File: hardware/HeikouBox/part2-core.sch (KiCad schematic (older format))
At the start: 20 parts, among them J201 Conn_02x05_Odd_Even, U201 HeikouBox-Core, U202 74HCU04, Y201 14.31818MHz, Y202 28.37516MHz

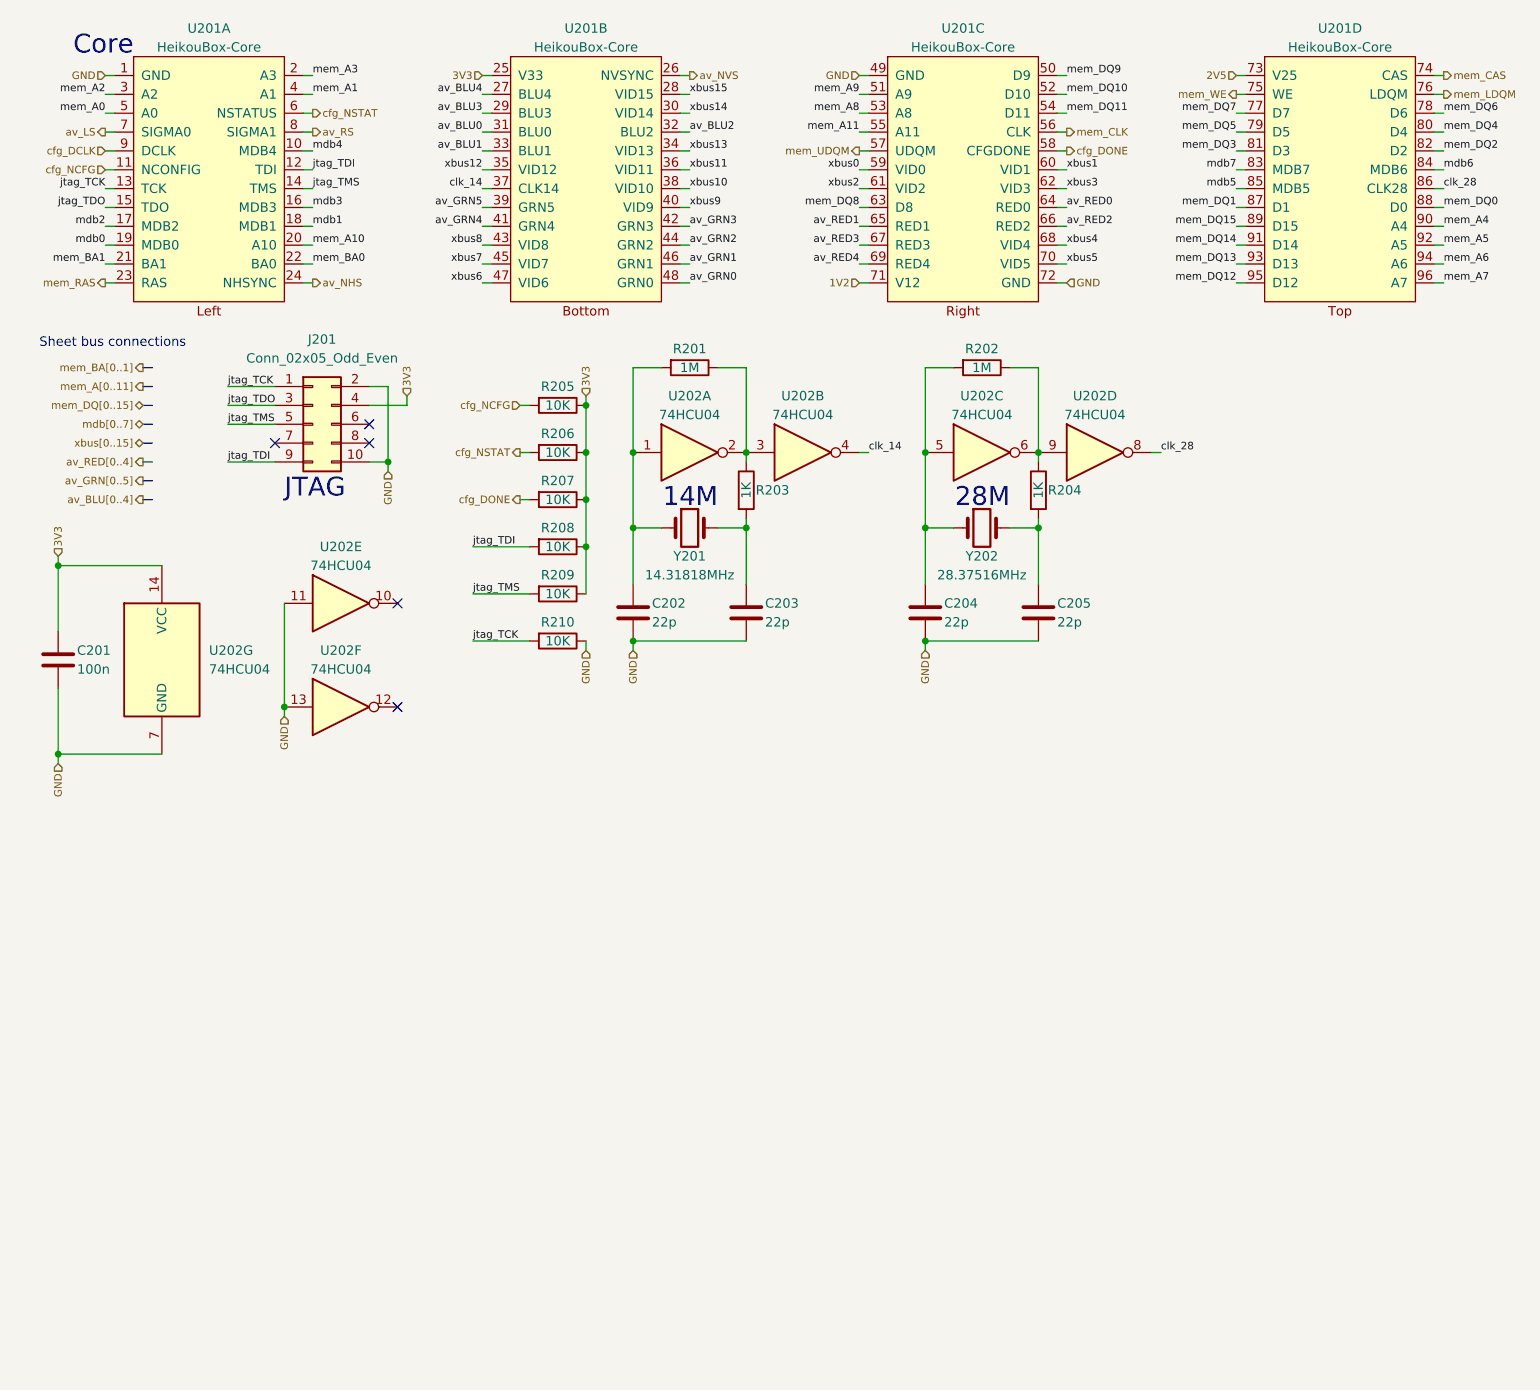
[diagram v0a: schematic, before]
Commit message: Replace MCU with blue pill, tidy up
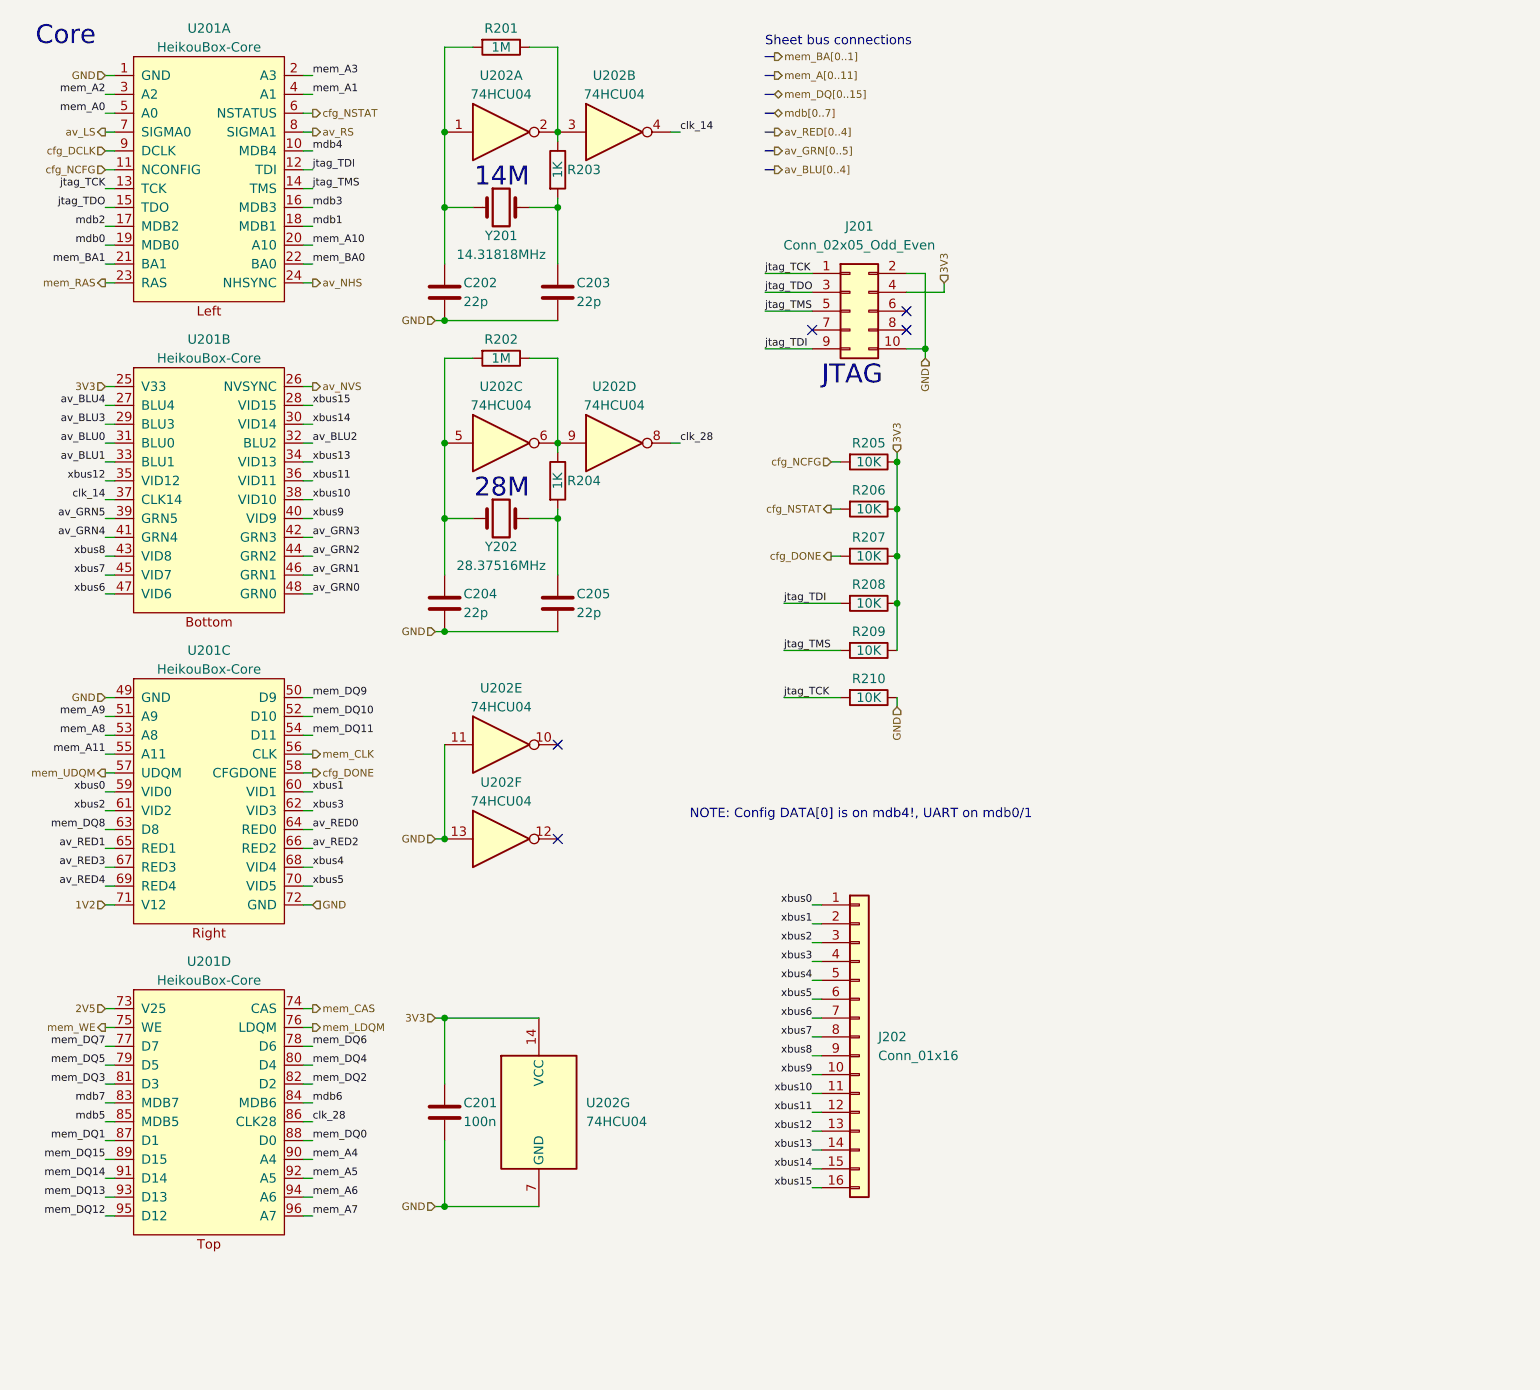
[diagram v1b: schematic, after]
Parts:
- added J202: Conn_01x16, Connector_PinSocket_2.54mm:PinSocket_1x16_P2.54mm_Vertical, symbol Connector_Generic:Conn_01x16
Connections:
- net xbus0: now also J202.1 (Pin_1)
- net xbus1: now also J202.2 (Pin_2)
- net xbus10: now also J202.11 (Pin_11)
- net xbus11: now also J202.12 (Pin_12)
- net xbus12: now also J202.13 (Pin_13)
- net xbus13: now also J202.14 (Pin_14)
- net xbus14: now also J202.15 (Pin_15)
- net xbus15: now also J202.16 (Pin_16)
- net xbus2: now also J202.3 (Pin_3)
- net xbus3: now also J202.4 (Pin_4)
- net xbus4: now also J202.5 (Pin_5)
- net xbus5: now also J202.6 (Pin_6)
- net xbus6: now also J202.7 (Pin_7)
- net xbus7: now also J202.8 (Pin_8)
- net xbus8: now also J202.9 (Pin_9)
- net xbus9: now also J202.10 (Pin_10)
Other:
- note added: "NOTE: Config DATA[0] is on mdb4!, UART on mdb0/1"
- moved on the sheet: C201, C202, C203, C204, C205, J201, R201, R202, R203, R204, R205, R206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

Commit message: Fix DRC, make netlist
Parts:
- U201: symbol KSK_HeikouBox:HeikouBox-Core -> KSK_HeikouBox:HeikouBox-Core-Socket
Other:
- moved on the sheet: C201, U202G
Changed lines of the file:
@@
 Core
 $Comp
-L KSK_HeikouBox:HeikouBox-Core U?
+L KSK_HeikouBox:HeikouBox-Core-Socket U?
 U 4 1 67C578BE
 P 1450 5650
@@
 av_BLU4
 $Comp
-L KSK_HeikouBox:HeikouBox-Core U?
+L KSK_HeikouBox:HeikouBox-Core-Socket U?
 U 2 1 67C578E9
 P 1450 2350
@@
 mdb3
 $Comp
-L KSK_HeikouBox:HeikouBox-Core U?
+L KSK_HeikouBox:HeikouBox-Core-Socket U?
 U 1 1 67C5790A
 P 1450 700
@@
 mdb6
 $Comp
-L KSK_HeikouBox:HeikouBox-Core U?
+L KSK_HeikouBox:HeikouBox-Core-Socket U?
 U 3 1 67C5791D
 P 1450 4000
@@
 $EndComp
 Wire Wire Line
-	4750 2850 4800 2850
-Wire Wire Line
-	4750 3100 4800 3100
-Wire Wire Line
-	4750 3350 4800 3350
-Wire Wire Line
-	4500 4100 4800 4100
+	4700 2850 4800 2850
+Wire Wire Line
+	4700 3100 4800 3100
+Wire Wire Line
+	4700 3350 4800 3350
+Wire Wire Line
+	4700 4100 4800 4100
 Text Notes 4700 2450 0    100  ~ 0
 JTAG
@@
 NoConn ~ 5150 2050
 NoConn ~ 5150 2150
-Wire Wire Line
-	5350 1950 5150 1950
 Wire Wire Line
 	5250 1850 5250 2250
@@
 NoConn ~ 3300 4350
 Wire Wire Line
-	2700 5800 3200 5800
+	2800 5800 3300 5800
 Wire Wire Line
 	2700 650  2700 1100
@@
 L Device:C C?
 U 1 1 67C57A73
-P 2700 6300
+P 2800 6300
 AR Path="/67C57A73" Ref="C?"  Part="1"
 AR Path="/71351D1D/67C57A73" Ref="C201"  Part="1"
 AR Path="/729F86A7/67C57A73" Ref="C?"  Part="1"
-F 0 "C201" H 2800 6350 50  0000 L CNN
-F 1 "100n" H 2800 6250 50  0000 L CNN
-F 2 "Capacitor_SMD:C_0603_1608Metric_Pad1.05x0.95mm_HandSolder" H 2738 6150 50  0001 C CNN
-F 3 "~" H 2700 6300 50  0001 C CNN
-	1    2700 6300
+F 0 "C201" H 2900 6350 50  0000 L CNN
+F 1 "100n" H 2900 6250 50  0000 L CNN
+F 2 "Capacitor_SMD:C_0603_1608Metric_Pad1.05x0.95mm_HandSolder" H 2838 6150 50  0001 C CNN
+F 3 "~" H 2800 6300 50  0001 C CNN
+	1    2800 6300
 	1    0    0    -1
 $EndComp
@@
 L 74xx:74HC04 U?
 U 7 1 67C57AA7
-P 3200 6300
+P 3300 6300
 AR Path="/67C57AA7" Ref="U?"  Part="7"
 AR Path="/71351D1D/67C57AA7" Ref="U202"  Part="7"
 AR Path="/729F86A7/67C57AA7" Ref="U?"  Part="7"
-F 0 "U202" H 3450 6350 50  0000 L CNN
-F 1 "74HCU04" H 3450 6250 50  0000 L CNN
-F 2 "Package_SO:SOIC-14_3.9x8.7mm_P1.27mm" H 3200 6300 50  0001 C CNN
-F 3 "https://assets.nexperia.com/documents/data-sheet/74HC_HCT04.pdf" H 3200 6300 50  0001 C CNN
-	7    3200 6300
+F 0 "U202" H 3550 6350 50  0000 L CNN
+F 1 "74HCU04" H 3550 6250 50  0000 L CNN
+F 2 "Package_SO:SOIC-14_3.9x8.7mm_P1.27mm" H 3300 6300 50  0001 C CNN
+F 3 "https://assets.nexperia.com/documents/data-sheet/74HC_HCT04.pdf" H 3300 6300 50  0001 C CNN
+	7    3300 6300
 	1    0    0    -1
 $EndComp
@@
 14M
 Wire Wire Line
-	5250 2300 5250 2250
-Text HLabel 5250 2300 3    40   Input ~ 0
+	5350 2250 5250 2250
+Text HLabel 5350 2250 2    40   Input ~ 0
 GND
 Connection ~ 5250 2250
-Text HLabel 4750 3350 0    40   Output ~ 0
+Text HLabel 4700 3350 0    40   Output ~ 0
 cfg_DONE
 Wire Wire Line
-	4500 3600 4800 3600
-Wire Wire Line
-	4500 3850 4800 3850
-Text HLabel 4750 3100 0    40   Output ~ 0
+	4700 3600 4800 3600
+Wire Wire Line
+	4700 3850 4800 3850
+Text HLabel 4700 3100 0    40   Output ~ 0
 cfg_NSTAT
-Text HLabel 4750 2850 0    40   Input ~ 0
+Text HLabel 4700 2850 0    40   Input ~ 0
 cfg_NCFG
 Wire Wire Line
@@
 Text HLabel 5100 2800 1    40   Input ~ 0
 3V3
-Text HLabel 5350 1900 1    40   Input ~ 0
+Text HLabel 5350 1950 2    40   Input ~ 0
 3V3
-Wire Wire Line
-	5350 1900 5350 1950
 Wire Wire Line
 	5100 4150 5100 4100
@@
 Text Label 2000 800  0    40   ~ 0
 mem_A3
-Text Label 4500 4100 0    40   ~ 0
+Text Label 4700 4100 2    40   ~ 0
 jtag_TCK
 Text Label 2000 1300 0    40   ~ 0
@@
 jtag_TDO
 Wire Wire Line
-	2700 5800 2650 5800
-Text HLabel 2650 5800 0    40   Input ~ 0
+	2800 5800 2700 5800
+Text HLabel 2700 5800 0    40   Input ~ 0
 3V3
 Wire Wire Line
 	2700 4350 2700 4850
 Wire Wire Line
-	2650 6800 2700 6800
-Text HLabel 2650 6800 0    40   Input ~ 0
+	2700 6800 2800 6800
+Text HLabel 2700 6800 0    40   Input ~ 0
 GND
 Wire Wire Line
-	3200 6800 2700 6800
-Connection ~ 2700 6800
-Wire Wire Line
-	2700 6800 2700 6450
+	3300 6800 2800 6800
+Connection ~ 2800 6800
+Wire Wire Line
+	2800 6800 2800 6450
 Wire Wire Line
 	2650 4850 2700 4850
@@
 GND
 Connection ~ 2700 4850
-Connection ~ 2700 5800
-Wire Wire Line
-	2700 6150 2700 5800
+Connection ~ 2800 5800
+Wire Wire Line
+	2800 6150 2800 5800
 Wire Wire Line
 	3150 650  3300 650
@@
 	1    0    0    -1
 $EndComp
-Text Label 4500 3850 0    40   ~ 0
+Text Label 4700 3850 2    40   ~ 0
 jtag_TMS
-Text Label 4500 3600 0    40   ~ 0
+Text Label 4700 3600 2    40   ~ 0
 jtag_TDI
 Text Notes 4000 4750 0    50   ~ 0
@@
 Text Label 4650 6700 2    40   ~ 0
 xbus15
+Wire Wire Line
+	5150 1950 5350 1950
 $EndSCHEMATC

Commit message: Mostly routed board
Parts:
- C201, C202, C203, C204, C205: footprint Capacitor_SMD:C_0603_1608Metric_Pad1.05x0.95mm_HandSolder -> Capacitor_SMD:C_0603_1608Metric_Pad1.08x0.95mm_HandSolder
- J202: value Conn_01x16 -> Conn_02x08_Odd_Even; footprint Connector_PinSocket_2.54mm:PinSocket_1x16_P2.54mm_Vertical -> Connector_PinHeader_2.54mm:PinHeader_2x08_P2.54mm_Vertical; symbol Connector_Generic:Conn_01x16 -> Connector_Generic:Conn_02x08_Odd_Even
- R201, R202, R203, R204, R205, R206, R207, R208, R209, R210: footprint Resistor_SMD:R_0603_1608Metric_Pad1.05x0.95mm_HandSolder -> Resistor_SMD:R_0603_1608Metric_Pad0.98x0.95mm_HandSolder
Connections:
- net GND: now also U202.5, U202.9; no longer U202.11, U202.13
- net clk_28: now also U202.10; no longer U202.8
- net at U202.12: now also R202.1, R204.1, U202.11
- net at C204.1, R202.2, Y202.1: now also U202.13; no longer U202.5
- now unconnected: U202.6
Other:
- moved on the sheet: J202, U202C, U202D, U202E, U202F

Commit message: Tidy up power nets
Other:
- moved on the sheet: J202, R205, R206, R207, R208, R209, R210
